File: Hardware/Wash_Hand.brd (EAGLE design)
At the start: 71.1 x 48.3 mm, 89 parts, among them IC1 LM358D, IC2 LP298XS, IC3 405016TSSOP, J1 I2C, J2 ICSP, J3 SPI, J4 9V_CONN, J5 EXT_VCC, J6 6_PIN_SERIAL_CABLEPTH, J8 2X6 FEMALE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

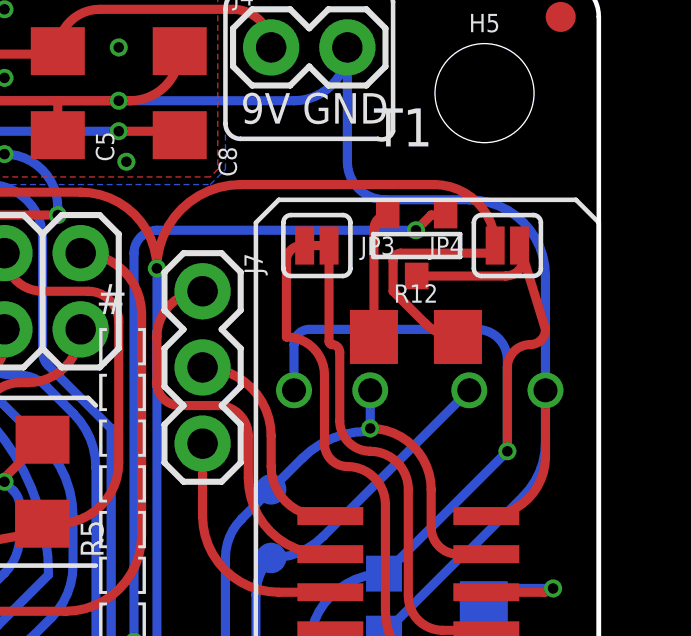
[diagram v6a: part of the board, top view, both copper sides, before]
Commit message: Board/Schematic: Add 1.2K resistor to transistor - in correct place
This fixes the "Board/Schematic: Add 1.2K resistor to transistor" and
adds the resistor on the correct side of the transitor.

Signed-off-by: Konrad Rzeszutek Wilk <konrad@kernel.org>
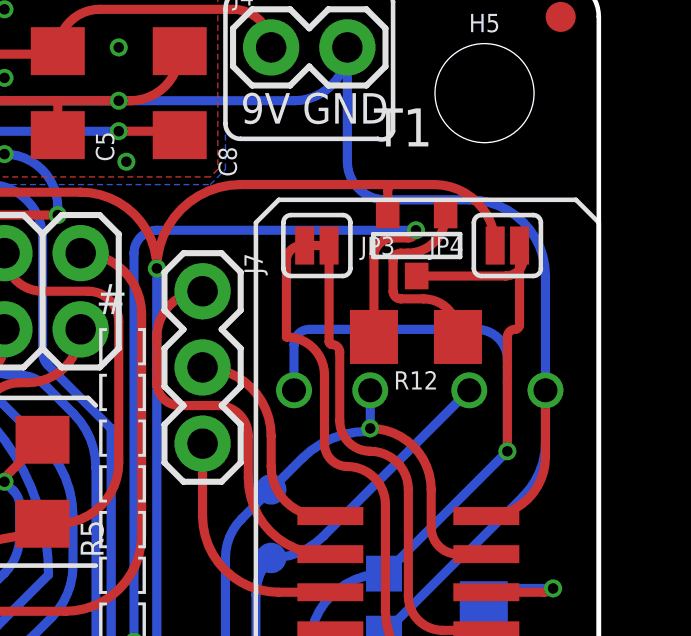
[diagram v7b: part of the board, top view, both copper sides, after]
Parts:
- turned R12 to 180 degrees
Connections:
- removed net N$19: R12.1, T1.2
- new net N$16: R12.1, T1.3
- net ON_OFF_PNP: now also R12.2; no longer T1.3
- net VCC: now also T1.2; no longer R12.2
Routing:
- net N$16: track 0.00 -> 6.27 mm
- net VCC: track 255.3 -> 249.0 mm
- net N$19: track 4.25 -> 0.00 mm
- net ON_OFF_PNP: track 62.0 -> 65.2 mm
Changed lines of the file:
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@@
 <attribute name="VALUE" x="39.878" y="34.163" size="0.6096" layer="27" font="vector" ratio="20"/>
 </element>
-<element name="R12" library="darnok_common" package="1206" value="1.2K" x="65.024" y="36.322" smashed="yes">
-<attribute name="NAME" x="65.024" y="37.465" size="0.6096" layer="25" font="vector" ratio="20" align="bottom-center"/>
-<attribute name="VALUE" x="65.024" y="35.179" size="0.6096" layer="27" font="vector" ratio="20" align="top-center"/>
+<element name="R12" library="darnok_common" package="1206" value="1.2K" x="65.024" y="36.322" smashed="yes" rot="R180">
+<attribute name="NAME" x="65.024" y="35.179" size="0.6096" layer="25" font="vector" ratio="20" rot="R180" align="bottom-center"/>
+<attribute name="VALUE" x="65.024" y="37.465" size="0.6096" layer="27" font="vector" ratio="20" rot="R180" align="top-center"/>
 </element>
 </elements>
@@
 <wire x1="64.262" y1="41.402" x2="65.6336" y2="41.402" width="0.3048" layer="1"/>
 <wire x1="65.6336" y1="41.402" x2="67.6656" y2="39.37" width="0.3048" layer="1" curve="-90"/>
-<contactref element="R12" pad="2"/>
-<wire x1="65.334865625" y1="36.773134375" x2="66.424" y2="36.322" width="0.3048" layer="1" curve="45"/>
-<wire x1="67.6656" y1="39.37" x2="67.4116" y2="39.116" width="0.3048" layer="1" curve="-90"/>
-<wire x1="64.516" y1="39.116" x2="64.262" y2="38.862" width="0.3048" layer="1" curve="90"/>
-<wire x1="64.262" y1="38.862" x2="64.262" y2="37.846" width="0.3048" layer="1"/>
-<wire x1="64.262" y1="37.846" x2="65.334865625" y2="36.773134375" width="0.3048" layer="1"/>
-<wire x1="67.4116" y1="39.116" x2="64.516" y2="39.116" width="0.3048" layer="1"/>
+<contactref element="T1" pad="2"/>
+<wire x1="64.0842" y1="40.386" x2="64.0842" y2="41.2242" width="0.3048" layer="1"/>
+<wire x1="64.0842" y1="41.2242" x2="64.262" y2="41.402" width="0.3048" layer="1" curve="-90"/>
 </signal>
 <signal name="0">
@@
 <wire x1="61.722" y1="25.4" x2="61.468" y2="25.654" width="0.3048" layer="16"/>
 <wire x1="68.4784" y1="39.37" x2="68.608434375" y2="38.949296875" width="0.3048" layer="1"/>
-<wire x1="68.608434375" y1="38.949296875" x2="69.342" y2="36.576" width="0.3048" layer="1"/>
-<wire x1="69.342" y1="36.576" x2="68.834" y2="36.068" width="0.3048" layer="1" curve="-90"/>
-<wire x1="68.834" y1="36.068" x2="68.072" y2="35.306" width="0.3048" layer="1" curve="90"/>
-<wire x1="68.072" y1="35.306" x2="68.072" y2="32.512" width="0.3048" layer="1"/>
+<wire x1="68.072" y1="35.306" x2="68.072" y2="34.798" width="0.3048" layer="1"/>
+<wire x1="68.072" y1="34.798" x2="68.072" y2="32.512" width="0.3048" layer="1"/>
 <wire x1="68.072" y1="32.512" x2="64.01391875" y2="28.45391875" width="0.3048" layer="16"/>
 <wire x1="64.01391875" y1="28.45391875" x2="63.961" y2="28.432" width="0.3048" layer="16" curve="-45"/>
@@
 <wire x1="65.0494" y1="38.354" x2="68.0131375" y2="38.354" width="0.3048" layer="1"/>
 <wire x1="68.0131375" y1="38.354" x2="68.608434375" y2="38.949296875" width="0.3048" layer="1" curve="90"/>
+<wire x1="68.4784" y1="39.37" x2="68.4784" y2="36.7284" width="0.3048" layer="1"/>
+<wire x1="68.4784" y1="36.7284" x2="68.326" y2="36.576" width="0.3048" layer="1" curve="-90"/>
+<wire x1="68.326" y1="36.576" x2="68.072" y2="36.322" width="0.3048" layer="1" curve="90"/>
+<wire x1="68.072" y1="36.322" x2="68.072" y2="35.306" width="0.3048" layer="1"/>
 </signal>
 <signal name="NEG_IN">
@@
 <signal name="ON_OFF_PNP">
 <contactref element="U2" pad="22"/>
-<contactref element="T1" pad="3"/>
-<wire x1="66.0146" y1="40.386" x2="65.532" y2="40.386" width="0.3048" layer="1"/>
-<wire x1="65.532" y1="40.386" x2="65.024" y2="39.878" width="0.3048" layer="1"/>
 <via x="65.024" y="39.878" extent="1-16" drill="0.35"/>
 <wire x1="31.2674" y1="11.754" x2="31.566" y2="11.754" width="0.3048" layer="1"/>
@@
 <wire x1="41.612421875" y1="26.162" x2="40.386" y2="25.654" width="0.3048" layer="1" curve="45"/>
 <via x="40.386" y="25.654" extent="1-16" drill="0.35"/>
+<contactref element="R12" pad="2"/>
+<wire x1="65.024" y1="39.878" x2="64.77" y2="39.624" width="0.3048" layer="1" curve="-90"/>
+<wire x1="64.77" y1="39.624" x2="64.262" y2="39.624" width="0.3048" layer="1"/>
+<wire x1="64.262" y1="39.624" x2="63.624" y2="38.986" width="0.3048" layer="1" curve="90"/>
+<wire x1="63.624" y1="38.986" x2="63.624" y2="36.322" width="0.3048" layer="1"/>
 </signal>
 <signal name="N$15">
@@
 <contactref element="U$5" pad="PIN$3"/>
 </signal>
-<signal name="N$19">
-<contactref element="T1" pad="2"/>
+<signal name="N$16">
+<contactref element="T1" pad="3"/>
 <contactref element="R12" pad="1"/>
-<wire x1="63.624" y1="36.322" x2="63.624" y2="39.9258" width="0.3048" layer="1"/>
-<wire x1="63.624" y1="39.9258" x2="64.0842" y2="40.386" width="0.3048" layer="1" curve="-90"/>
+<wire x1="66.424" y1="36.322" x2="66.424" y2="36.446" width="0.3048" layer="1"/>
+<wire x1="66.424" y1="36.446" x2="65.278" y2="37.592" width="0.3048" layer="1" curve="90"/>
+<wire x1="65.278" y1="37.592" x2="64.516" y2="37.592" width="0.3048" layer="1"/>
+<wire x1="64.516" y1="37.592" x2="64.262" y2="37.846" width="0.3048" layer="1" curve="-90"/>
+<wire x1="64.262" y1="38.862" x2="64.516" y2="39.116" width="0.3048" layer="1" curve="-90"/>
+<wire x1="64.516" y1="39.116" x2="64.7446" y2="39.116" width="0.3048" layer="1"/>
+<wire x1="64.7446" y1="39.116" x2="66.0146" y2="40.386" width="0.3048" layer="1" curve="90"/>
+<wire x1="64.262" y1="37.846" x2="64.262" y2="38.862" width="0.3048" layer="1"/>
 </signal>
 </signals>

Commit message: RELEASE-1.4-rc3
Signed-off-by: Konrad Rzeszutek Wilk <konrad@kernel.org>
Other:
- board text added: "v1.4-rc3"
- board text removed: "v1.4-rc2"
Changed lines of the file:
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@@
 <circle x="8.636" y="38.862" radius="0.254" width="0.254" layer="25"/>
 <circle x="8.636" y="38.862" radius="0.567959375" width="0.1524" layer="25"/>
-<text x="33.02" y="5.842" size="1.778" layer="26" ratio="14" rot="MR0">v1.4-rc2</text>
+<text x="33.02" y="5.842" size="1.778" layer="26" ratio="14" rot="MR0">v1.4-rc3</text>
 <text x="54.356" y="18.796" size="1.016" layer="25" ratio="14">#
 [  ]
